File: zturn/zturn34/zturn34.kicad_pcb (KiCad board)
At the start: 4 copper layers, 189.9 x 54 mm, 37 parts, among them U1 74AXP4T245, U10 74AXP4T245, U11 74AXP4T245, U12 74AXP4T245, U2 74AXP4T245, U3 74AXP4T245, U4 74AXP4T245, U5 74AXP4T245, U9 74AXP4T245

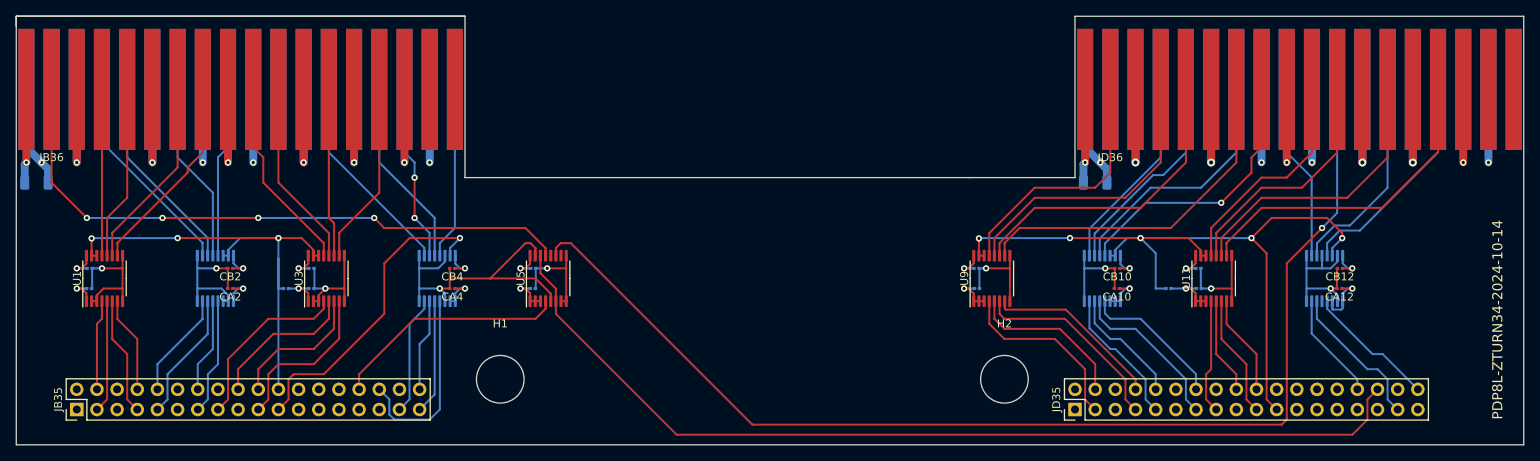
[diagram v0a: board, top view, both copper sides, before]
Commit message: update zturn34,35 pcbs - move 10uF caps, add fiducials
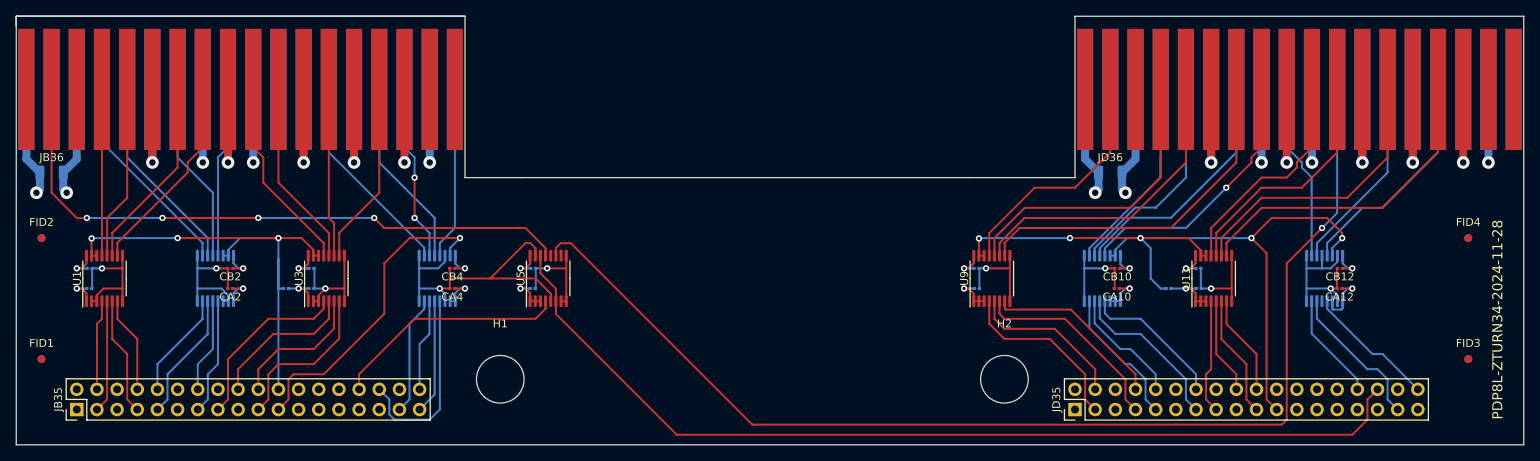
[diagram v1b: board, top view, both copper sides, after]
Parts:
- added FID1: Fiducial, Fiducial:Fiducial_1mm_Mask2mm, F.Cu at (3.17, 43.2)
- added FID2: Fiducial, Fiducial:Fiducial_1mm_Mask2mm, F.Cu at (3.17, 27.9)
- added FID3: Fiducial, Fiducial:Fiducial_1mm_Mask2mm, F.Cu at (182.9, 43.2)
- added FID4: Fiducial, Fiducial:Fiducial_1mm_Mask2mm, F.Cu at (182.9, 27.9)
- added FID5: Fiducial, Fiducial:Fiducial_1mm_Mask2mm, B.Cu at (3.17, 43.2)
- added FID6: Fiducial, Fiducial:Fiducial_1mm_Mask2mm, B.Cu at (3.17, 27.9)
- added FID7: Fiducial, Fiducial:Fiducial_1mm_Mask2mm, B.Cu at (182.9, 43.2)
- added FID8: Fiducial, Fiducial:Fiducial_1mm_Mask2mm, B.Cu at (182.9, 27.9)
- moved C3 2.29 mm to (137.8, 19.7), turned to 0 degrees
- moved C1 2.29 mm to (4.45, 19.7), turned to 0 degrees
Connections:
- JB36 pad A1: GND -> unconnected-(JB36-PadA1)
- JD36 pad A1: GND -> unconnected-(JD36-PadA1)
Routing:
- net +5V: track 52.3 -> 68.9 mm
- net GND: track 336.1 -> 324.4 mm, vias 29 -> 27
- net /pBTP2: track 22.3 -> 15.0 mm
- net /jINPUTBUS_05: track 28.1 -> 20.8 mm
- net /j_IO_SKIP: track 22.2 -> 14.9 mm
- net /pMA03: track 25.4 -> 18.1 mm
- net /jINPUTBUS_00: track 31.7 -> 30.2 mm
- net /jINPUTBUS_01: track 36.3 -> 37.4 mm
- net /j_AC_CLEAR: track 25.8 -> 24.7 mm
- net /jINPUTBUS_04: track 27.4 -> 26.3 mm
- net /jINPUTBUS_10: track 26.5 -> 27.3 mm
- net /j_EA: track 78.3 -> 79.1 mm
- net /jINPUTBUS_11: track 31.8 -> 31.1 mm
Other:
- board text added: "PDP8L-ZTURN34-2024-11-28"
- board text removed: "PDP8L-ZTURN34-2024-10-14"
